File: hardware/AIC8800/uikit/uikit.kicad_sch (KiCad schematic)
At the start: 40 parts, among them J1 Conn_01x20, J2 Conn_01x20, J3 Conn_01x10, J4 Conn_01x06, J5 USB_C_Receptacle_USB2.0, J6 Micro_SD_Card_Det, J7 PJ-393-USA, U1 AIC1000A, U2 CH340N

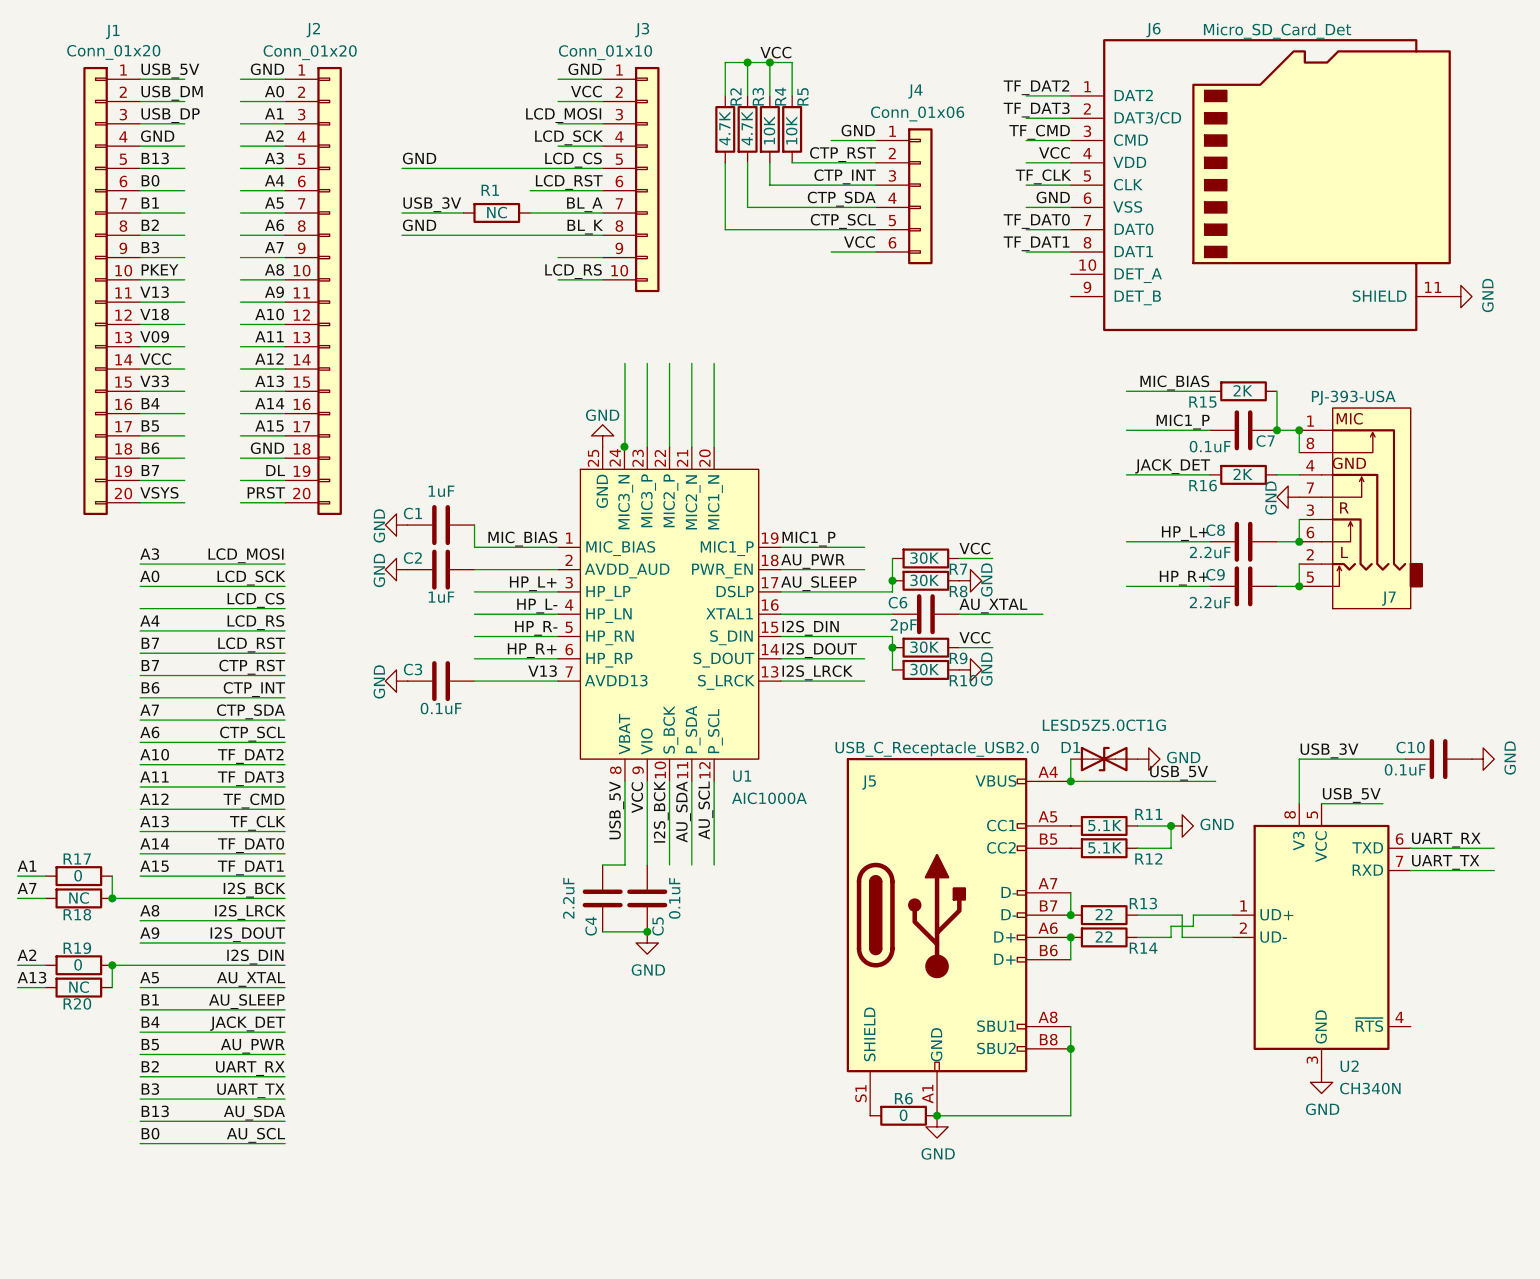
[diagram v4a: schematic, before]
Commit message: [hardware/aic8800/uikit] add speaker
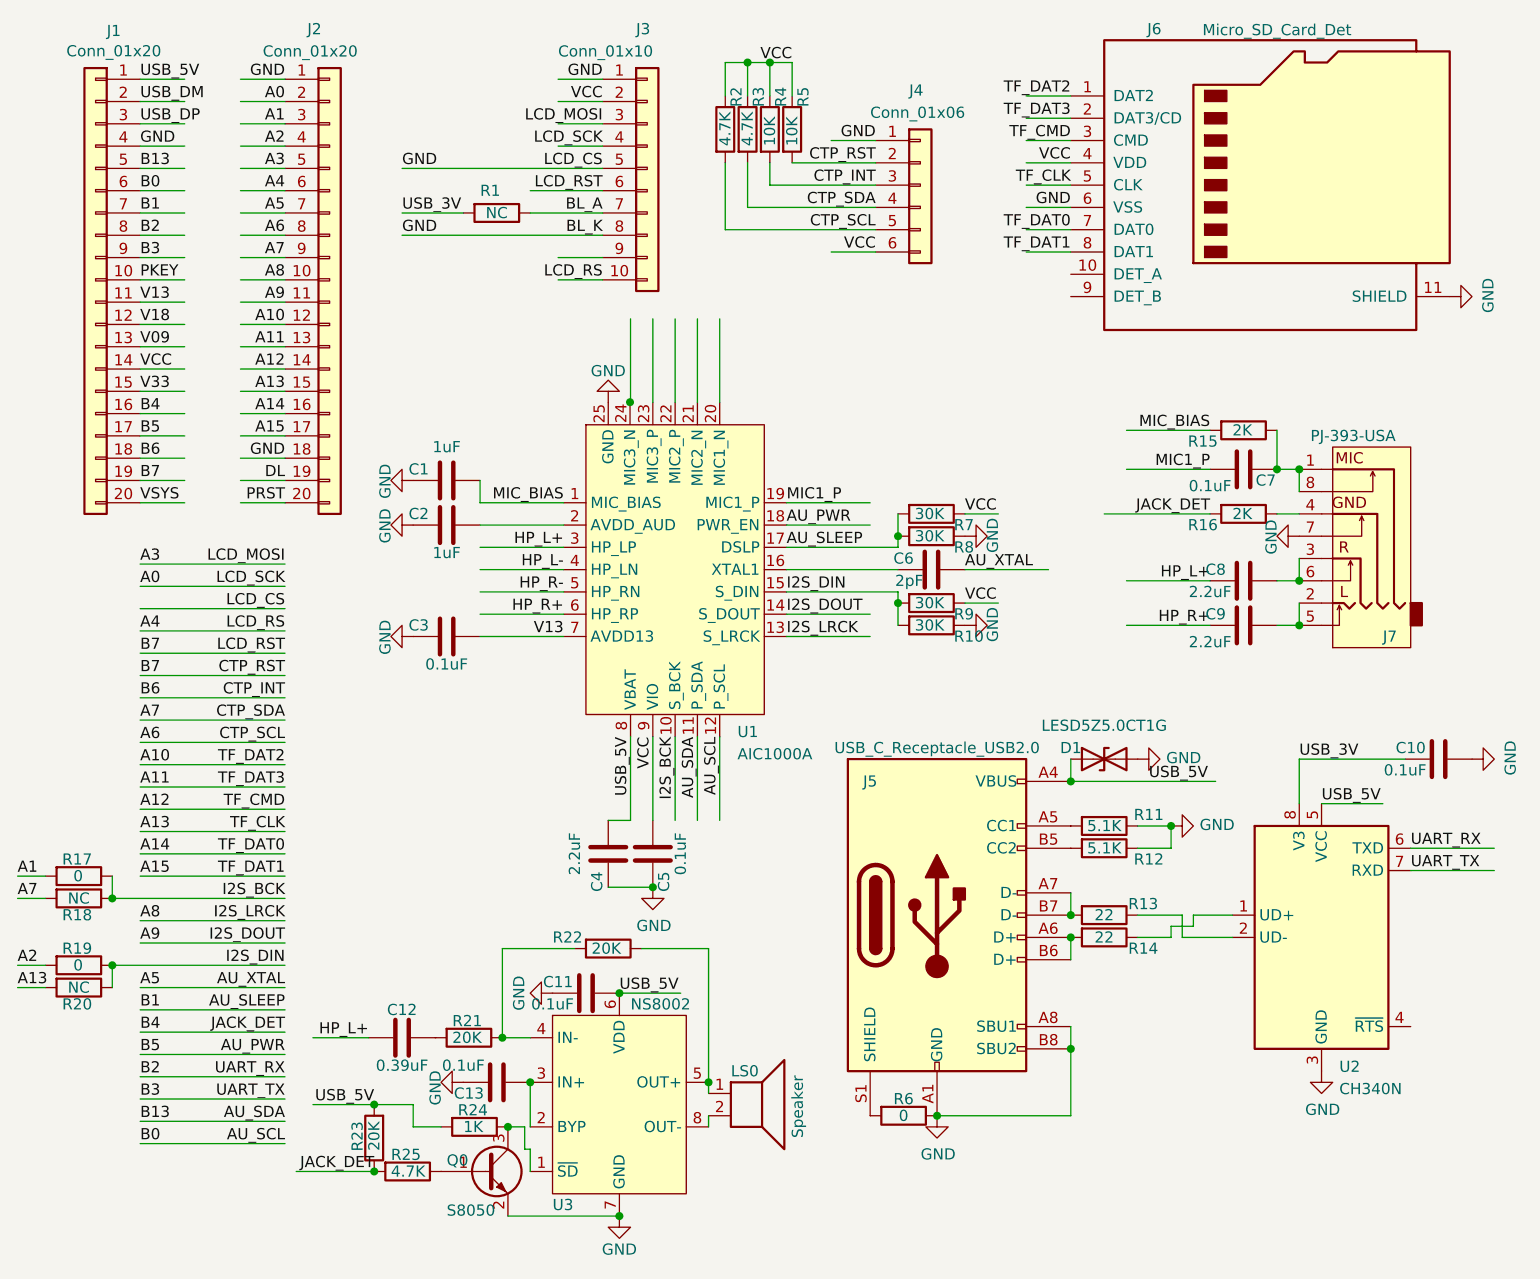
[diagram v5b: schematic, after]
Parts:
- added C11, C13: 0.1uF, Capacitor_SMD:C_0402_1005Metric, symbol Device:C
- added C12: 0.39uF, Capacitor_SMD:C_0402_1005Metric, symbol Device:C
- added LS0: Speaker, Connector_PinHeader_2.54mm:PinHeader_1x02_P2.54mm_Vertical, symbol Device:Speaker
- added Q0: S8050, Package_TO_SOT_SMD:SOT-23, symbol Transistor_BJT:S8050
- added R21, R22, R23: 20K, Resistor_SMD:R_0402_1005Metric, symbol Device:R
- added R24: 1K, Resistor_SMD:R_0402_1005Metric, symbol Device:R
- added R25: 4.7K, Resistor_SMD:R_0402_1005Metric, symbol Device:R
- added U3: NS8002, Package_SO:SOP-8_3.9x4.9mm_P1.27mm, symbol VSF:NS8002
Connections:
- net B4: now also R23.1, R25.2
- net GND: now also C11.1, C13.1, Q0.2 (E), U3.7 (GND)
- net HP_L+: now also C12.1
- net USB_5V: now also C11.2, R23.2, R24.2, U3.6 (VDD)
- new net: C12.2, R21.2
- new net: LS0.1, R22.1, U3.5 (OUT+)
- new net: R21.1, R22.2, U3.4 (IN-)
- new net: Q0.1 (B), R25.1
- new net: Q0.3 (C), R24.1, U3.1 (~{SD})
- new net: C13.2, U3.2 (BYP), U3.3 (IN+)
- new net: LS0.2, U3.8 (OUT-)
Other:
- moved on the sheet: C1, C2, C3, C4, C5, C6, C7, C8, C9, J7, R10, R15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

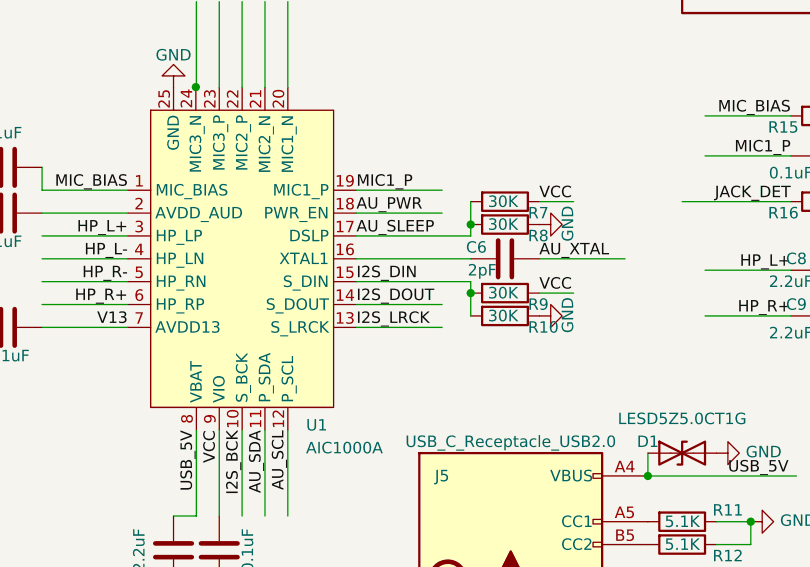
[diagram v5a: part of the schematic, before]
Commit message: [hardware/aic8800/uikit] fix i2s
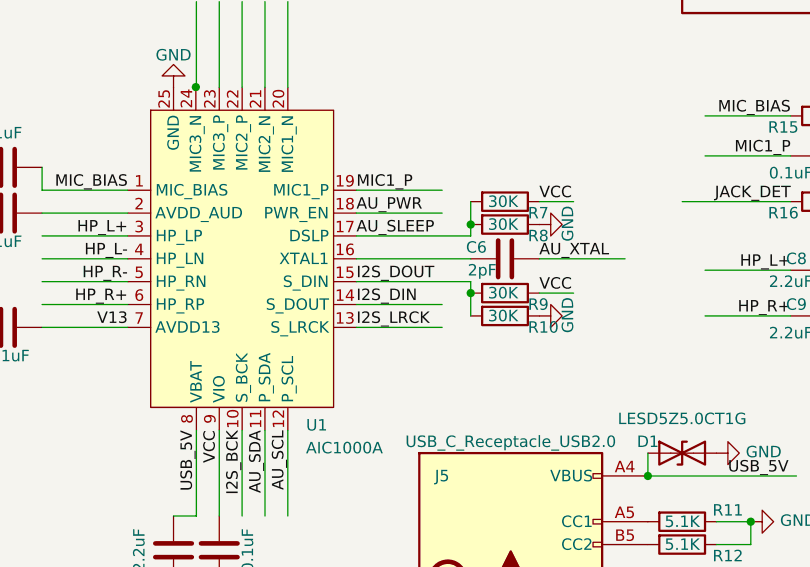
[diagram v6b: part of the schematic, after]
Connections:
- net A9: now also R10.2, R9.2, U1.15 (S_DIN); no longer U1.14 (S_DOUT)
- net I2S_DIN: now also U1.14 (S_DOUT); no longer R10.2, R9.2, U1.15 (S_DIN)
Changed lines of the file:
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@@
     (effects (font (size 1.27 1.27)) (justify right bottom))
   )
-  (label "I2S_DIN" (at 105.41 85.09 0)
+  (label "I2S_DIN" (at 105.41 87.63 0)
     (effects (font (size 1.27 1.27)) (justify left bottom))
   )
@@
     (effects (font (size 1.27 1.27)) (justify right bottom))
   )
-  (label "I2S_DOUT" (at 105.41 87.63 0)
+  (label "I2S_DOUT" (at 105.41 85.09 0)
     (effects (font (size 1.27 1.27)) (justify left bottom))
   )
@@
       (effects (font (size 1.27 1.27)) (justify left) hide)
     )
-    (pin "2")
-    (pin "1")
+    (pin "1")
+    (pin "2")
     (pin "3")
   )

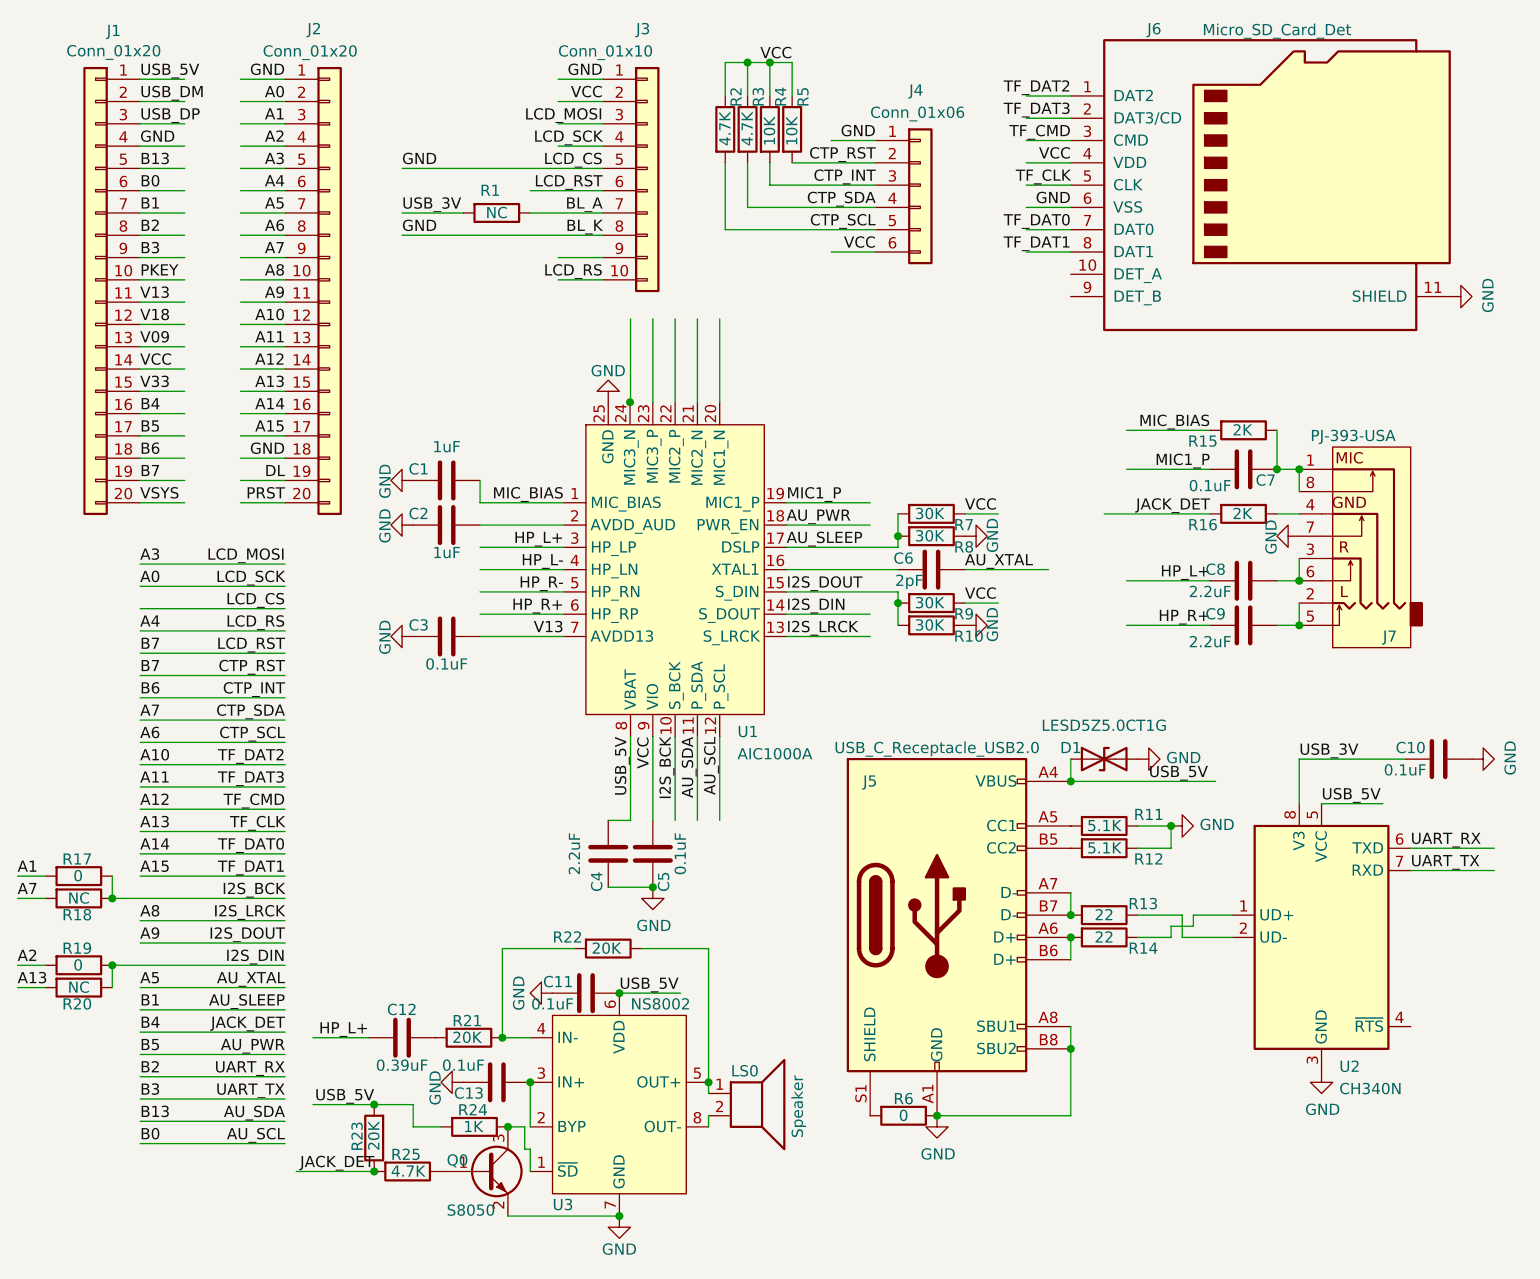
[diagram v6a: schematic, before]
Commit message: [hardware/aic8800/uikit] update JACK_DET
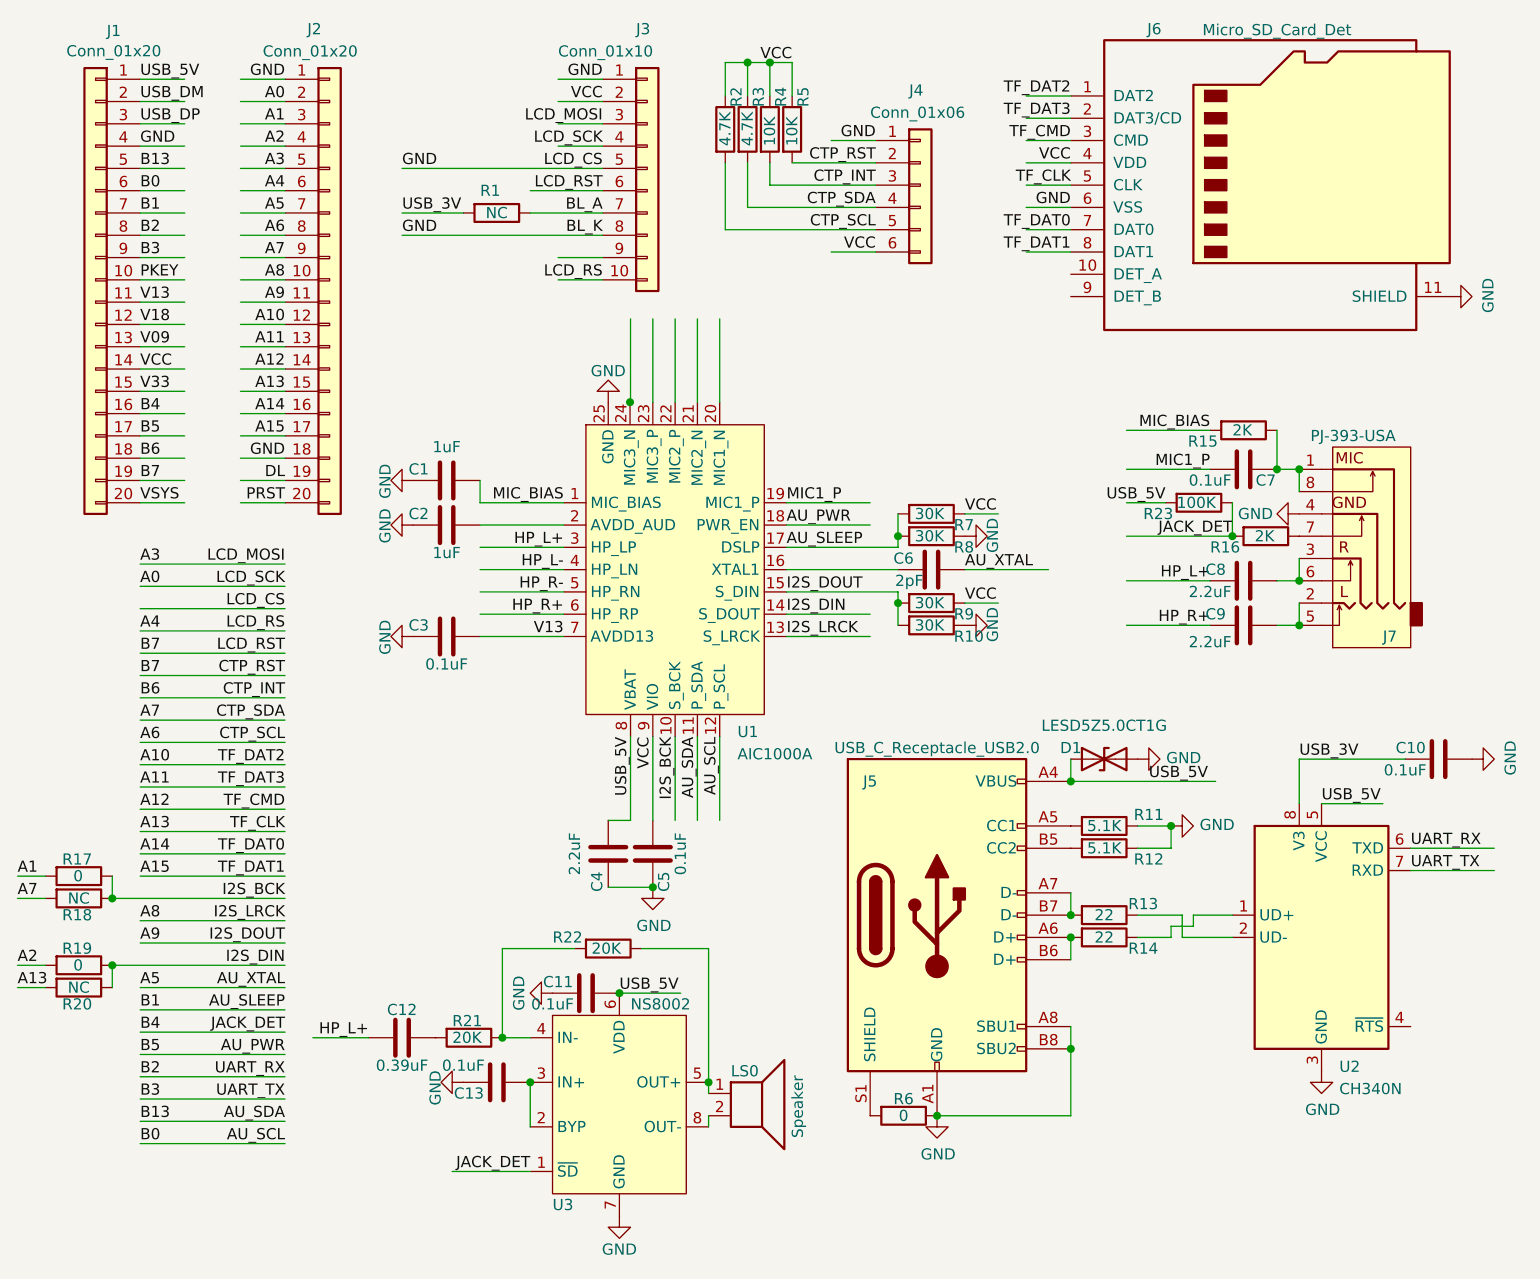
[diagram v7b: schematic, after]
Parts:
- removed Q0: S8050, Package_TO_SOT_SMD:SOT-23, symbol Transistor_BJT:S8050
- removed R24: 1K, Resistor_SMD:R_0402_1005Metric, symbol Device:R
- removed R25: 4.7K, Resistor_SMD:R_0402_1005Metric, symbol Device:R
- R23: value 20K -> 100K
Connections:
- net B4: now also U3.1 (~{SD})
- net GND: now also J7.4; no longer J7.7
- net at R16.1: now also J7.7; no longer J7.4
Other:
- moved on the sheet: R16, R23

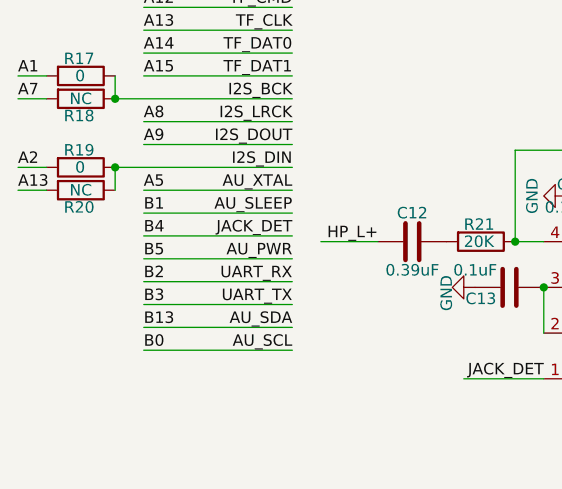
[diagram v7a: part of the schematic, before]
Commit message: [hardware/aic8800/uikit] PB0 can only be used as input
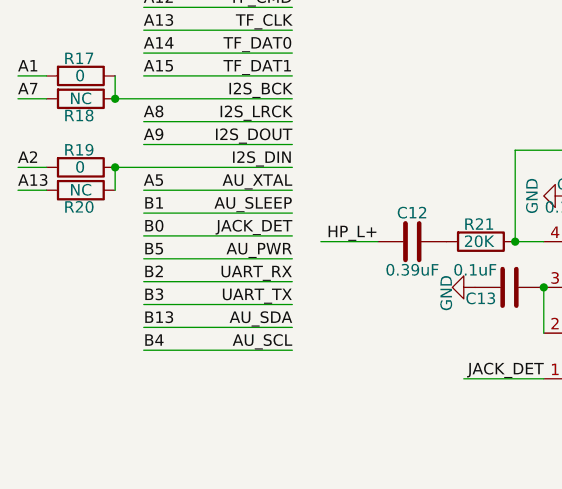
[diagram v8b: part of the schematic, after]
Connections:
- net AU_SCL: now also J1.16 (Pin_16); no longer J1.6 (Pin_6)
- net B4 renamed B0
- net B0: now also J1.6 (Pin_6); no longer J1.16 (Pin_16)
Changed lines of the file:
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@@
     (effects (font (size 1.27 1.27)) (justify right bottom))
   )
-  (label "B0" (at 31.75 147.955 0)
+  (label "B0" (at 31.75 135.255 0)
     (effects (font (size 1.27 1.27)) (justify left bottom))
   )
@@
     (effects (font (size 1.27 1.27)) (justify right bottom))
   )
-  (label "B4" (at 31.75 135.255 0)
+  (label "B4" (at 31.75 147.955 0)
     (effects (font (size 1.27 1.27)) (justify left bottom))
   )
